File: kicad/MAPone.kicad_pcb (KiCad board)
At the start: 2 copper layers, 70 x 30 mm, 34 parts, among them J1 BARREL_JACK, J2 USB-Micro, P1 CONN_1, P2 CONN_1, P3 CONN_1, P4 CONN_1, SW1 RST, U1 7805, U2 ATMEGA328-P, X1 16MHz

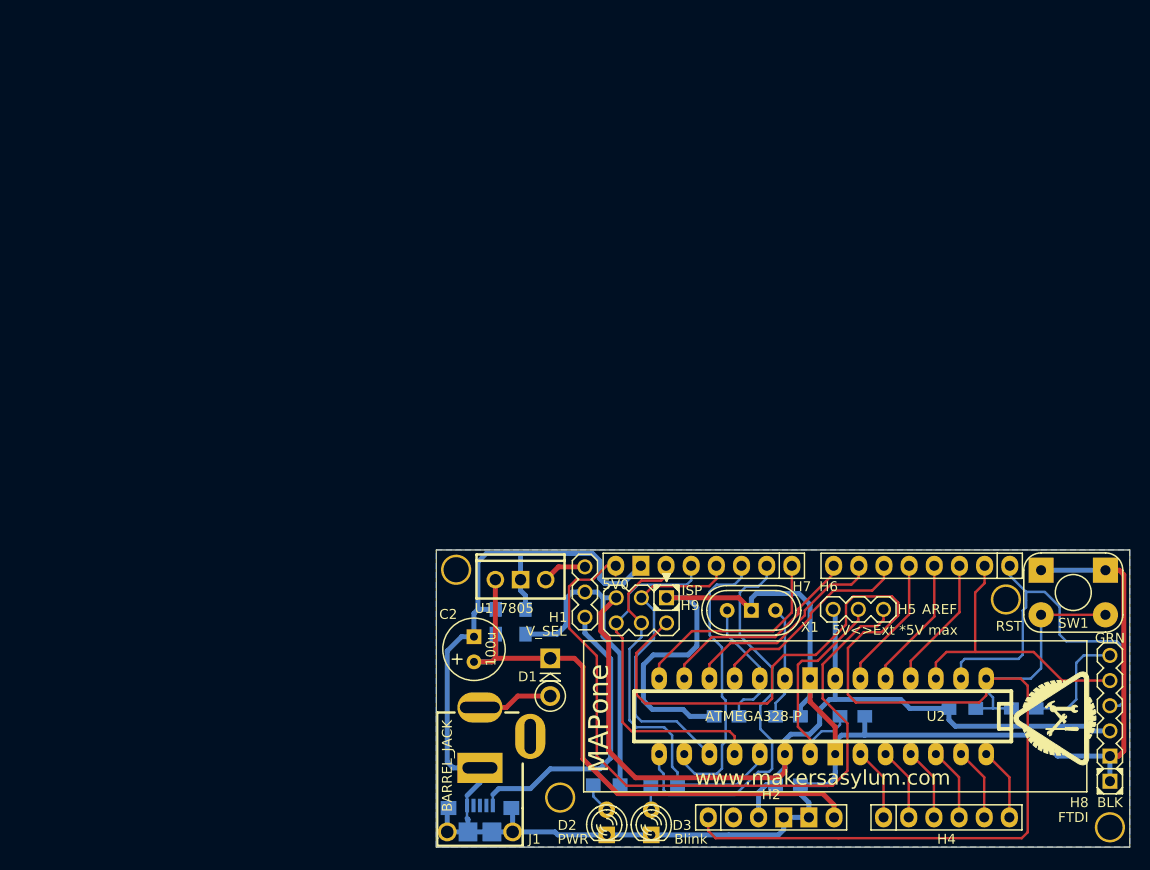
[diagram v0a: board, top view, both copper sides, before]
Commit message: MAPone Schematic, PCB, BoM complete. USB<>UART PCB Pending
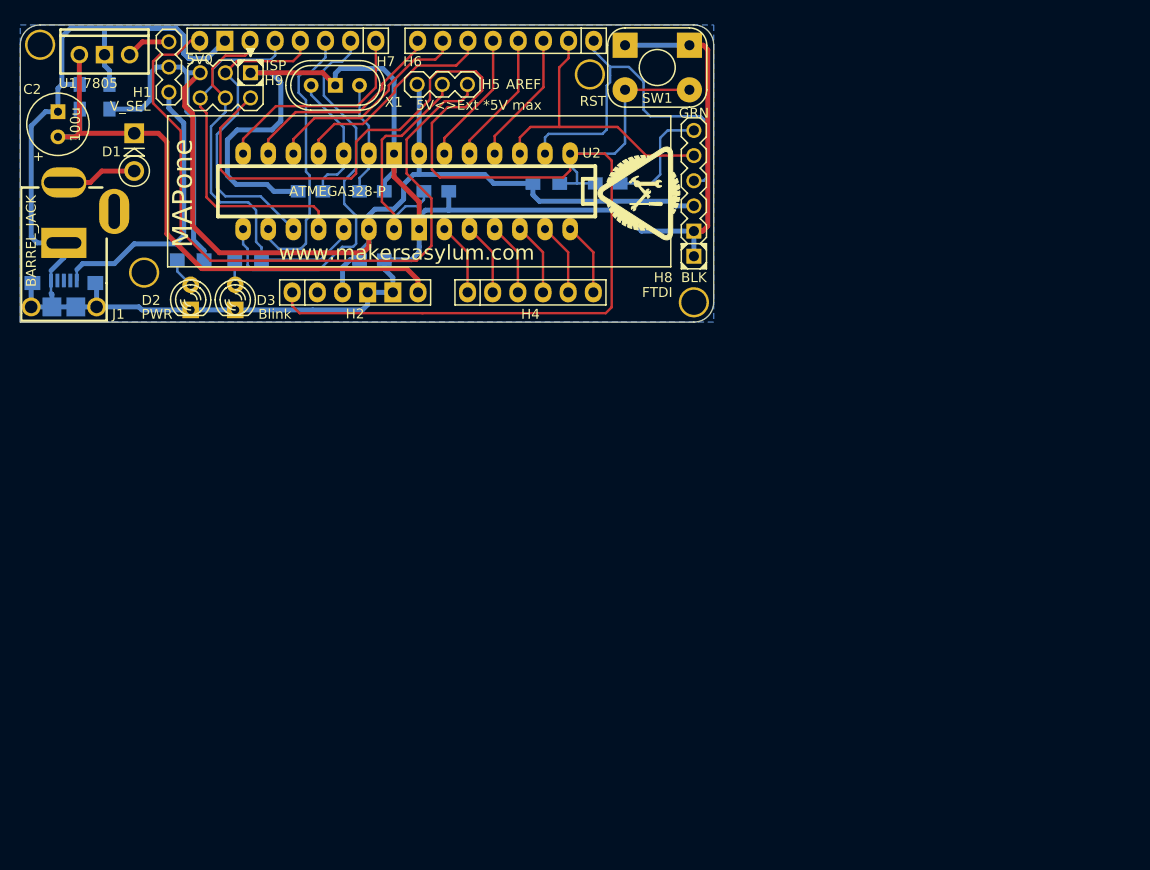
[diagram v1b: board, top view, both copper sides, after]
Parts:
- R2, R3: value 1k -> 300E
- moved C6 67.6 mm to (89.3, 46.0)
- moved J1 67.6 mm to (34.4, 52.0)
- moved J2 67.6 mm to (34.4, 55.8)
- moved SW1 67.6 mm to (94.3, 34.3)
- moved C1 67.6 mm to (65.5, 53.7)
- moved C2 67.6 mm to (33.8, 41.3)
- moved C3 67.6 mm to (36.0, 37.2)
- moved C4 67.6 mm to (39.0, 37.2)
- moved C5 67.6 mm to (72.0, 46.8)
- moved C7 67.6 mm to (65.5, 46.8)
- moved C8 67.6 mm to (59.3, 46.8)
- moved D1 67.6 mm to (41.5, 42.8)
- moved D2 67.6 mm to (47.2, 57.5)
- moved D3 67.6 mm to (51.7, 57.5)
- moved G*** 67.6 mm to (92.5, 47.0)
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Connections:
- H2 pad 2: (no net) -> /3V3
- J1 pad 3: (no net) -> Net-(J1-Pad3)
- J2 pad 2: (no net) -> Net-(J2-Pad2)
- J2 pad 3: (no net) -> Net-(J2-Pad3)
- J2 pad 4: (no net) -> Net-(J2-Pad4)
- P1 pad 1: (no net) -> Net-(P1-Pad1)
- P2 pad 1: (no net) -> Net-(P2-Pad1)
- P3 pad 1: (no net) -> Net-(P3-Pad1)
- P4 pad 1: (no net) -> Net-(P4-Pad1)
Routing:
- net /V_USB: track 29.8 -> 28.4 mm
- net /SS_P: track 29.1 -> 28.1 mm
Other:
- outline, holes or cut-outs redrawn
- board text added: "* disable when using H8 or H9"
- board text added: "NOTES : 1. Arduino headers are arranged in same sequence as Duemilenova 2. Gap between headers is 25.4mm (1.0") against 48.26mm (1.9") on Duemilenova. 3. Four mounting holes, drilled to 3.125mm. 4. All SMD parts are on bottom layer. 5. For U2, ATMega-328P, use either regular DIP socket, or ZIF socket."

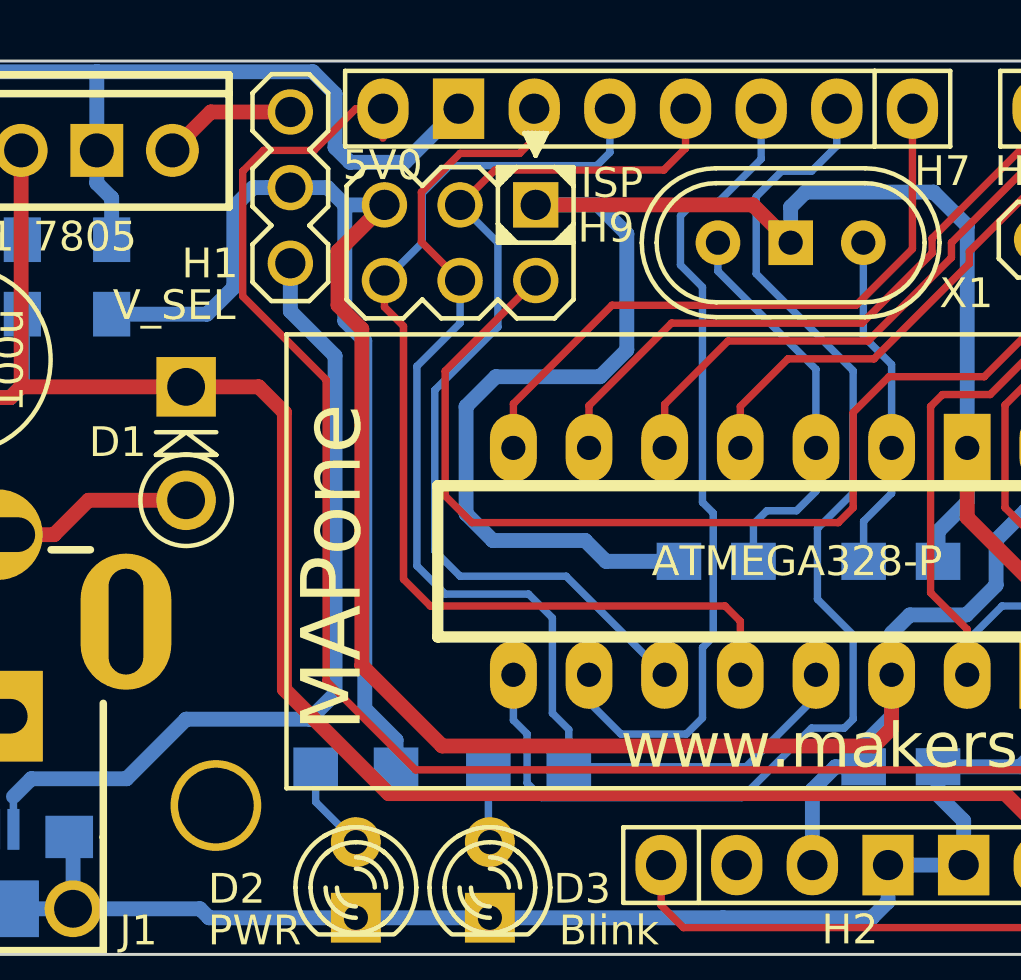
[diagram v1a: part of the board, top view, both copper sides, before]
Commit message: MAPone Schematic, PCB, BoM complete. USB<>UART PCB Pending
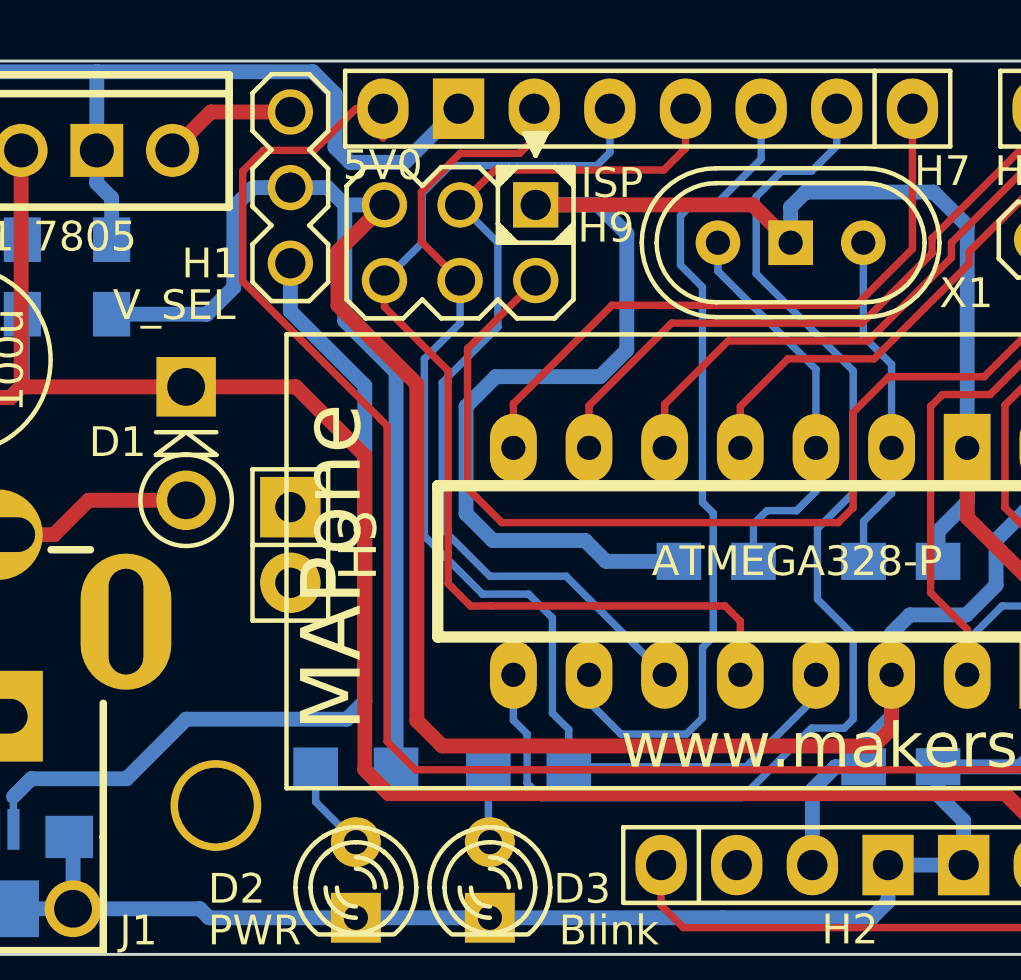
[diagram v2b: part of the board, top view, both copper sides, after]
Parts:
- added H3: LiPo_7V2, MAPone.pretty:Pin_Header_Straight_1x02, F.Cu at (45.0, 46.2)
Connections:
- H2 pad 2: /3V3 -> (no net)
- J1 pad 3: Net-(J1-Pad3) -> (no net)
- J2 pad 2: Net-(J2-Pad2) -> (no net)
- J2 pad 3: Net-(J2-Pad3) -> (no net)
- J2 pad 4: Net-(J2-Pad4) -> (no net)
- P1 pad 1: Net-(P1-Pad1) -> (no net)
- P2 pad 1: Net-(P2-Pad1) -> (no net)
- P3 pad 1: Net-(P3-Pad1) -> (no net)
- P4 pad 1: Net-(P4-Pad1) -> (no net)
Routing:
- net /V_USB: track 28.4 -> 30.0 mm
- net /RST: track 150.1 -> 148.8 mm
- net /SCK: track 39.7 -> 38.8 mm
- net /MOSI_P: track 32.2 -> 31.4 mm
- net /MISO: track 35.8 -> 35.0 mm
- net /V_IN: track 62.0 -> 62.8 mm

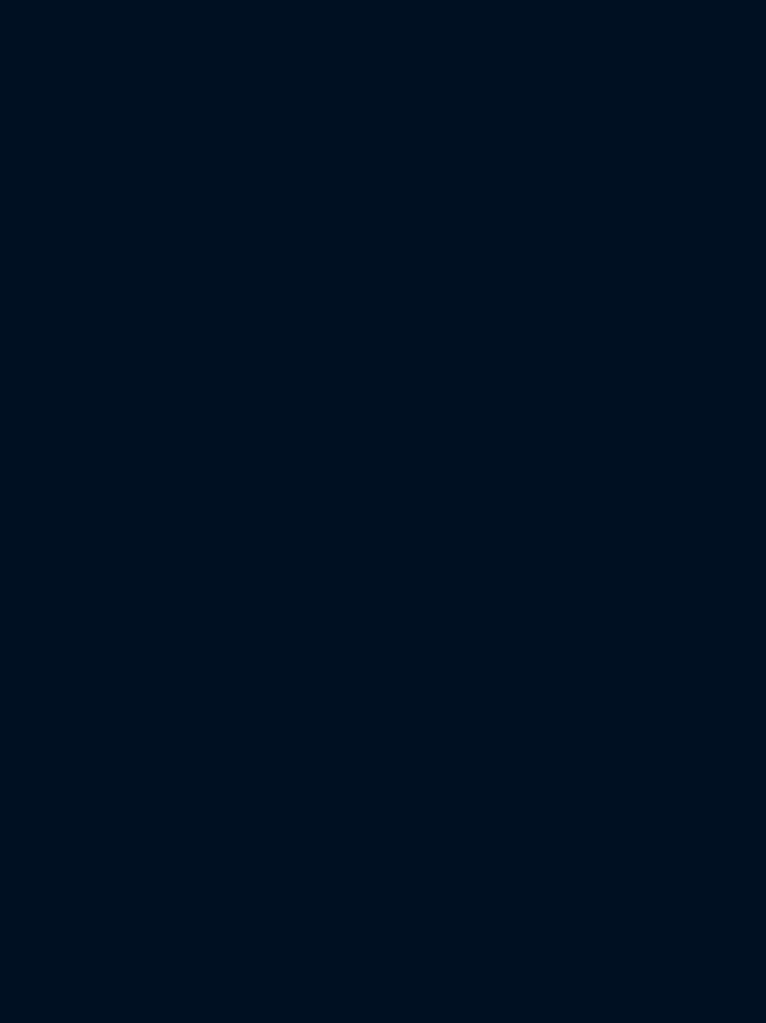
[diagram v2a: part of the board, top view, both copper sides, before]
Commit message: MAPone Schematic, PCB, BoM complete. USB<>UART PCB work in progress
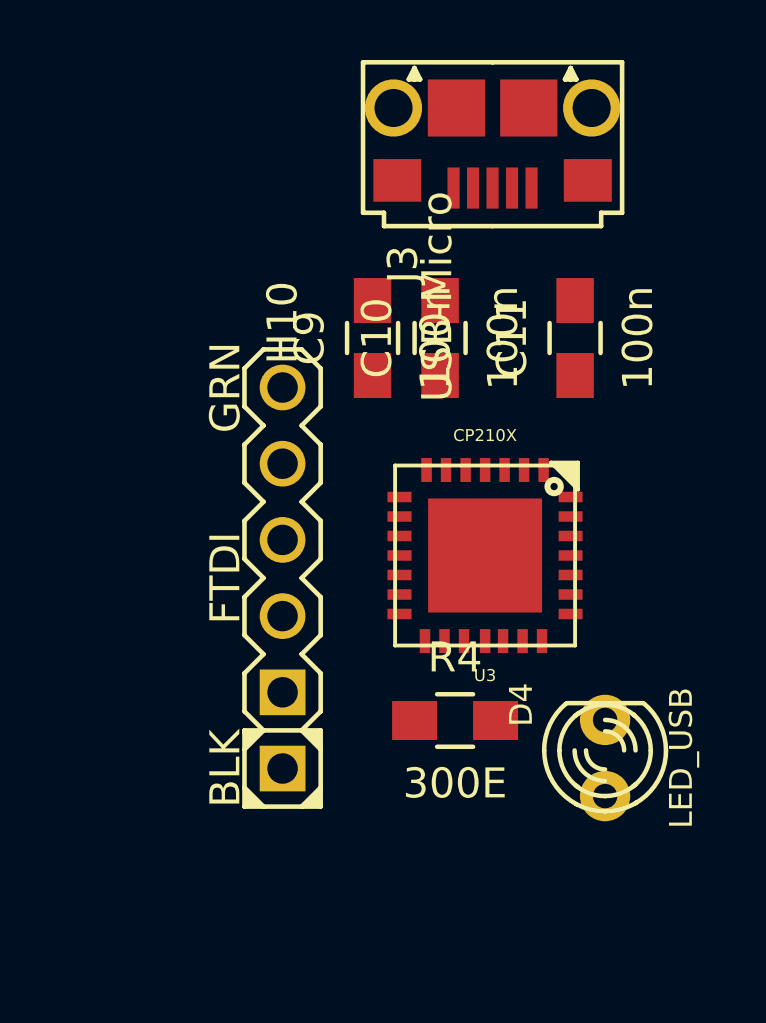
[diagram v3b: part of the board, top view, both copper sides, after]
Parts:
- added C10: 100n, MAPone.pretty:C_0805_HandSoldering, F.Cu at (126.5, 38.8)
- added C11: 100n, MAPone.pretty:C_0805_HandSoldering, F.Cu at (131.0, 38.8)
- added C9: 100n, MAPone.pretty:C_0805_HandSoldering, F.Cu at (124.2, 38.8)
- added D4: LED_USB, MAPone.pretty:LED-3MM, F.Cu at (132.0, 52.8)
- added H10: FTDI, MAPone.pretty:Header_FTDI, F.Cu at (121.2, 46.8)
- added J3: USB-Micro, MAPone.pretty:USB_B_Micro, F.Cu at (128.2, 33.8)
- added R4: 300E, MAPone.pretty:R_0805_HandSoldering, F.Cu at (127.0, 51.5)
- added U3: CP210X, MAPone.pretty:qfn-28, F.Cu at (128.0, 46.0)

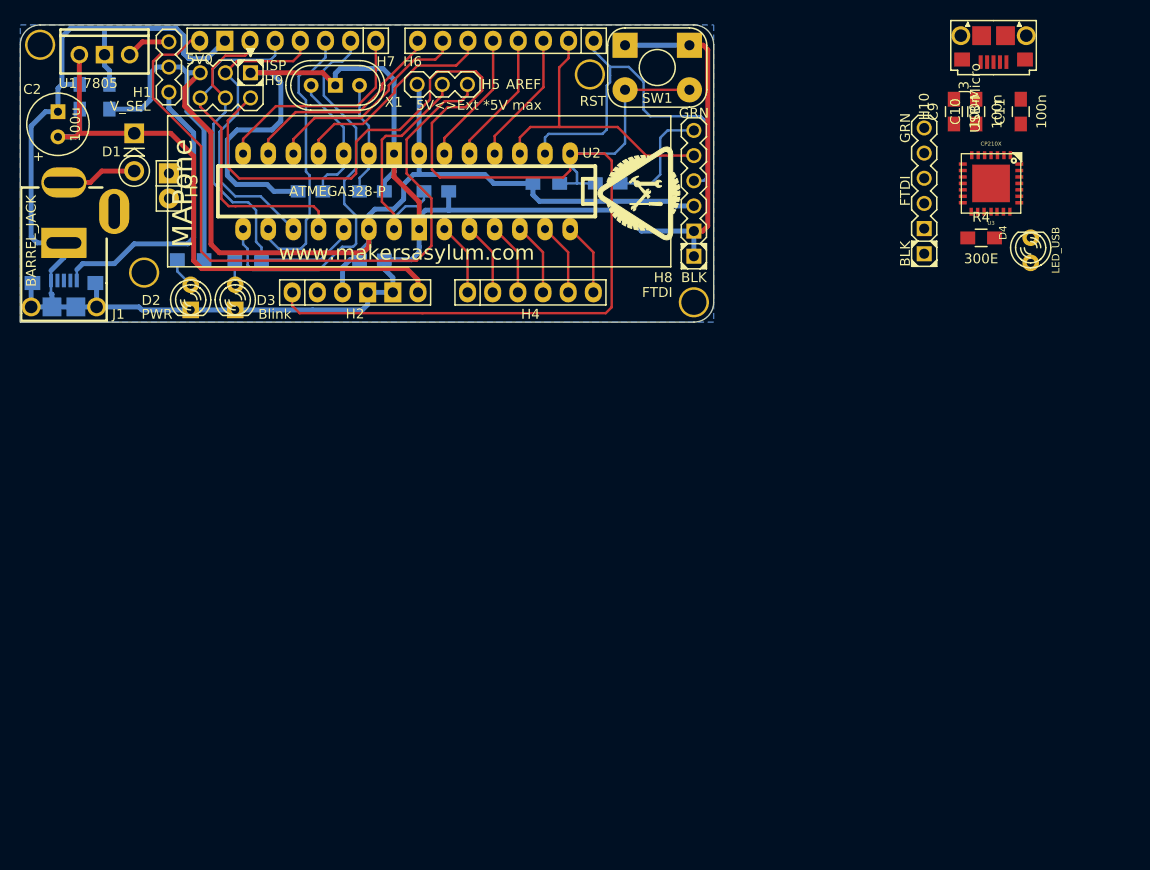
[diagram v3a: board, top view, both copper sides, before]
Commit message: MAPone Schematic, PCB, BoM complete. USB<>UART PCB work in progress
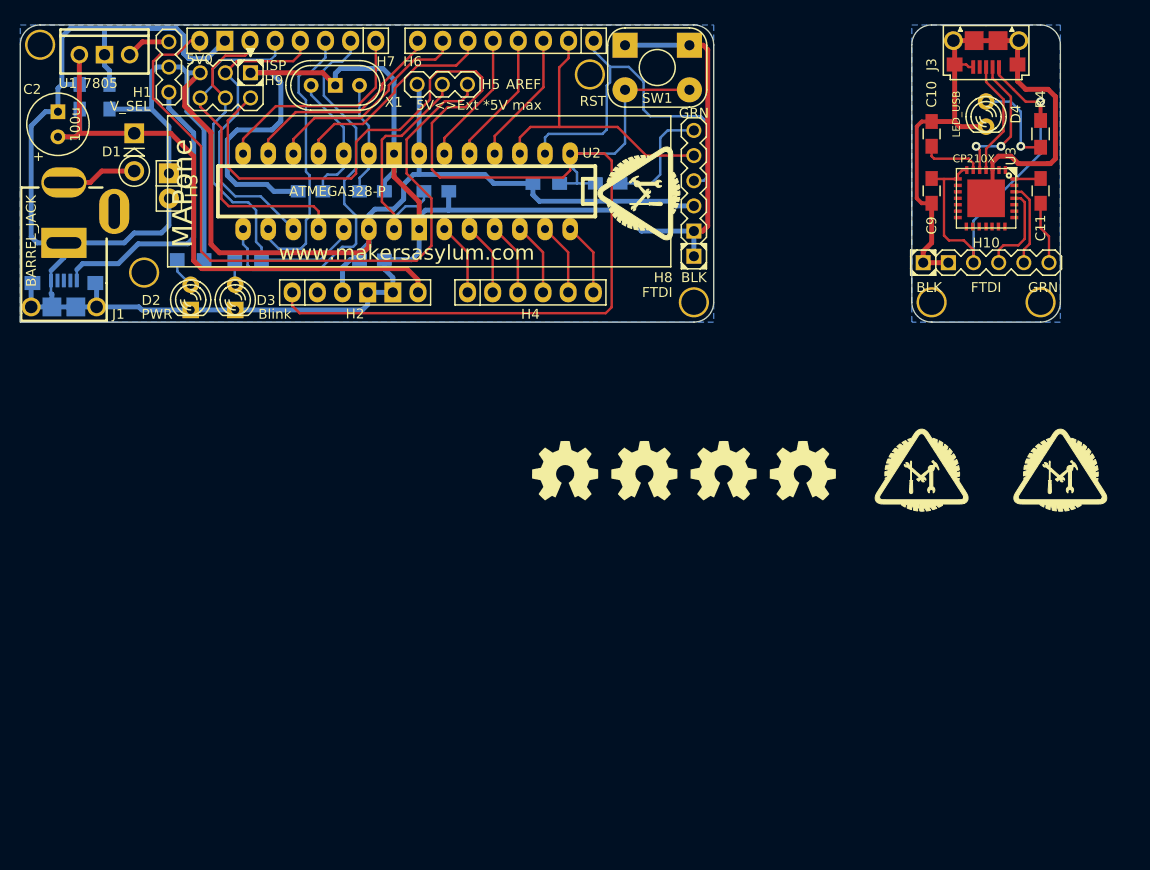
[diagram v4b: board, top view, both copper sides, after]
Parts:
- added P5: CONN_1, MAPone.pretty:vite_3mm, F.Cu at (133.0, 58.0)
- added P6: CONN_1, MAPone.pretty:vite_3mm, F.Cu at (122.0, 58.0)
- added Z3: CONN_1, MAPone.pretty:MA_Logo2, F.Cu at (121.0, 75.0)
- added Z4: CONN_1, MAPone.pretty:MA_Logo2, F.Cu at (135.0, 75.0)
- added Z5: CONN_1, MAPone:OSHW_6mm, F.Cu at (109.0, 75.0)
- added Z6: CONN_1, MAPone:OSHW_6mm, F.Cu at (101.0, 75.0)
- added Z7: CONN_1, MAPone:OSHW_6mm, F.Cu at (93.0, 75.0)
- added Z8: CONN_1, MAPone:OSHW_6mm, F.Cu at (85.0, 75.0)
- Z1, Z2: renamed from G***; value LOGO -> CONN_1
- moved D4 14.5 mm to (127.5, 39.0), turned to 270 degrees
- moved R4 12.1 mm to (133.0, 41.0), turned to 270 degrees
- moved H10 9.57 mm to (127.5, 54.0), turned to 0 degrees
- moved C9 8.31 mm to (122.0, 46.8), turned to 270 degrees
- moved C11 8.25 mm to (133.0, 46.8), turned to 270 degrees
- moved C10 5.03 mm to (122.0, 41.0)
- moved U3 1.58 mm to (127.5, 47.5)
- moved J3 0.90 mm to (127.5, 34.2)
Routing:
- net GND: track 239.2 -> 325.9 mm
- net /USB_UART/5V: track 0.00 -> 42.6 mm, vias 0 -> 1
- net /USB_UART/D-: track 0.00 -> 14.2 mm, vias 0 -> 2
- net /USB_UART/D+: track 0.00 -> 11.8 mm
- net Net-(D4-Pad1): track 0.00 -> 9.46 mm, vias 0 -> 1
- net /USB_UART/RXD: track 0.00 -> 9.28 mm
- net /USB_UART/TXD: track 0.00 -> 8.48 mm
- net /5V: track 127.7 -> 134.7 mm
- net Net-(C11-Pad2): track 0.00 -> 6.35 mm
- net /USB_UART/3V3: track 0.00 -> 6.19 mm
- net /USB_UART/RST: track 0.00 -> 2.67 mm
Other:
- board size 70 x 30 mm -> 105 x 30 mm
